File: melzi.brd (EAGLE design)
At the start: 208.3 x 49.5 mm, 121 parts, among them IC5 7805DT, IC6 ATMEGA1284P, IC7 4050D, IC8 FT232RL-BASICSSOP, M1 RFP30N06LE, M2 RFP30N06LE, M3 RFP30N06LE, Q1 16MHZ, U1 A4982, U2 A4982, U3 A4982, U4 A4982, X1 MICROSD, X2 MINI-USB-SHIELD-UX60-MB-5ST

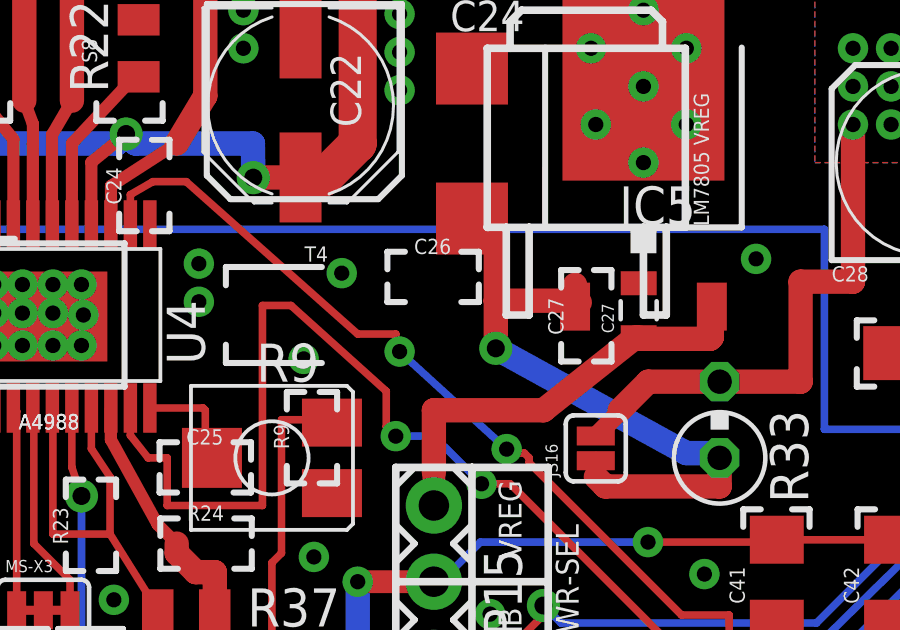
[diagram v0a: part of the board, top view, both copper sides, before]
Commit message: Added 0.33uF upstream of 5V reg.  Specified 4.7uF cap in parallel as 30V.
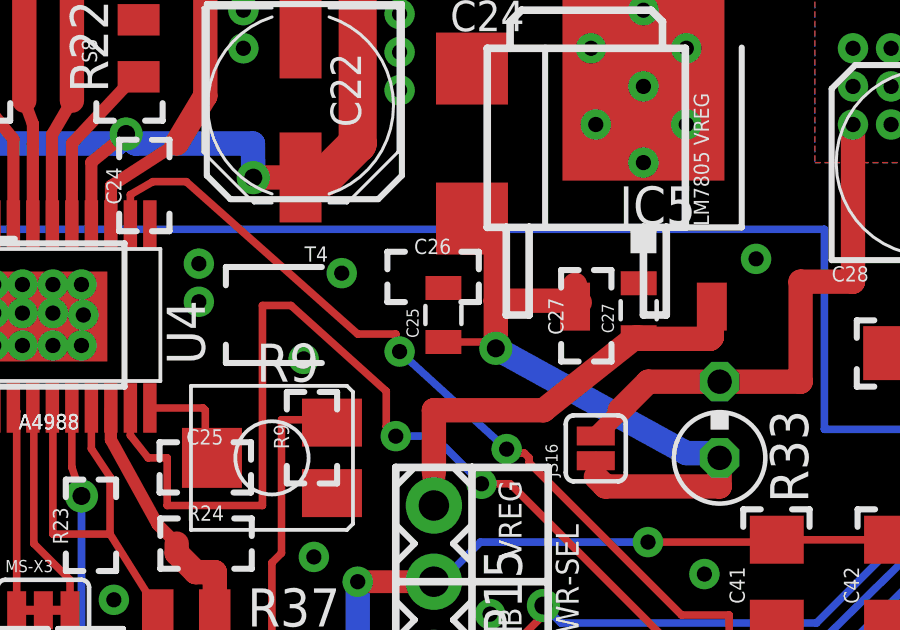
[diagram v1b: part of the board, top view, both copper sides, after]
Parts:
- added C25: .33uf, SparkFun:0805
- C24: value 4.7 uF -> 4.7 uF 30V
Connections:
- net GND: now also C25.2
- net N$36: now also C25.1
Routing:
- net N$36: track 22.6 -> 24.6 mm
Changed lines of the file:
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@@
 <attribute name="VALUE" x="89.74" y="14.035" size="1.27" layer="27" font="vector" ratio="10" rot="R180"/>
 </element>
-<element name="C24" library="rcl" package="SMC_C" value="4.7 uF" x="92.71" y="31.115" smashed="yes" rot="R90">
+<element name="C24" library="rcl" package="SMC_C" value="4.7 uF 30V" x="92.71" y="31.115" smashed="yes" rot="R90">
 <attribute name="NAME" x="94.45625" y="35.8775" size="1.016" layer="25" rot="R180"/>
 <attribute name="VALUE" x="95.5675" y="35.8775" size="1.016" layer="27" rot="R180"/>
 </element>
+<element name="C25" library="SparkFun" package="0805" value=".33uf" x="91.7575" y="25.4" rot="R90"/>
 </elements>
 <signals>
@@
 <via x="105.50525" y="3.175" extent="1-16" drill="0.508" diameter="1.016"/>
 <via x="154.33675" y="13.36675" extent="1-16" drill="0.508" diameter="1.016"/>
+<contactref element="C25" pad="2"/>
 </signal>
 <signal name="VCC" class="1">
@@
 <wire x1="96.2025" y1="25.87625" x2="93.50375" y2="25.87625" width="0.8128" layer="1"/>
 <wire x1="96.8375" y1="20.0025" x2="96.8375" y2="20.5431" width="0.6096" layer="1"/>
+<contactref element="C25" pad="1"/>
+<wire x1="91.7575" y1="24.5" x2="93.50375" y2="24.5" width="0.254" layer="1"/>
+<wire x1="93.50375" y1="24.5" x2="93.50375" y2="24.28875" width="0.254" layer="1"/>
 </signal>
 <signal name="N$3">

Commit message: "Made in the UK" added to silkscreen.
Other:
- board text added: "Made in the UK"
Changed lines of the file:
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@@
 <text x="89.8525" y="16.98625" size="0.6096" layer="49" rot="R90">VREG</text>
 <text x="89.8525" y="14.44625" size="0.6096" layer="49" rot="R90">USB</text>
+<text x="8.09625" y="4.1275" size="1.016" layer="49">Made in the UK</text>
 </plain>
 <attributes>
